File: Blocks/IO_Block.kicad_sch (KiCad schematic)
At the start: 3 parts

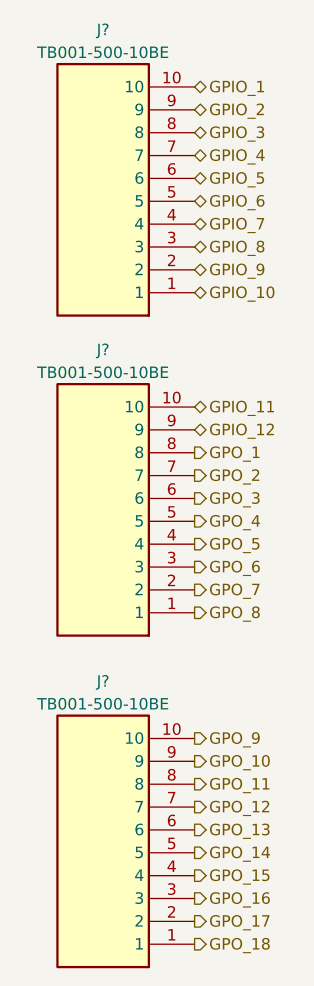
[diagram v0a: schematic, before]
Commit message: Automate library addition * Added script to automagically extract samacsys libraries and put them in corresponding folders. * Note: Requires zsh
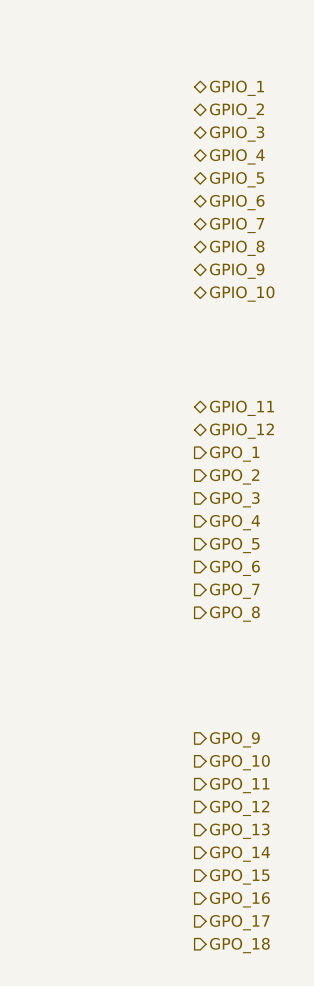
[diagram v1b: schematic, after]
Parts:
- removed J? (x3): TB001-500-10BE, LIB_TB001-500-10BE:SHDR10W100P0X500_1X10_5000X900X1250P, symbol TB001-500-10BE:TB001-500-10BE
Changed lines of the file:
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@@
     (effects (font (size 1.27 1.27)) (justify left))
   )
-  (symbol (lib_id "TB001-500-10BE:TB001-500-10BE") (at 86.36 153.67 180) (unit 1)
-    (in_bom yes) (on_board yes) (dnp no) (fields_autoplaced)
-    (property "Reference" "J?" (at 76.2 124.46 0)
-      (effects (font (size 1.27 1.27)))
-    )
-    (property "Value" "TB001-500-10BE" (at 76.2 127 0)
-      (effects (font (size 1.27 1.27)))
-    )
-    (property "Footprint" "LIB_TB001-500-10BE:SHDR10W100P0X500_1X10_5000X900X1250P" (at 69.85 58.75 0)
-      (effects (font (size 1.27 1.27)) (justify left top) hide)
-    )
-    (property "Datasheet" "https://componentsearchengine.com/Datasheets/1/TB001-500-10BE.pdf" (at 69.85 -41.25 0)
-      (effects (font (size 1.27 1.27)) (justify left top) hide)
-    )
-    (property "Height" "12.5" (at 69.85 -241.25 0)
-      (effects (font (size 1.27 1.27)) (justify left top) hide)
-    )
-    (property "Mouser Part Number" "490-TB001-500-10BE" (at 69.85 -341.25 0)
-      (effects (font (size 1.27 1.27)) (justify left top) hide)
-    )
-    (property "Mouser Price/Stock" "https://www.mouser.co.uk/ProductDetail/CUI-Devices/TB001-500-10BE?qs=vLWxofP3U2zH1ZAwWBP5mg%3D%3D" (at 69.85 -441.25 0)
-      (effects (font (size 1.27 1.27)) (justify left top) hide)
-    )
-    (property "Manufacturer_Name" "CUI Devices" (at 69.85 -541.25 0)
-      (effects (font (size 1.27 1.27)) (justify left top) hide)
-    )
-    (property "Manufacturer_Part_Number" "TB001-500-10BE" (at 69.85 -641.25 0)
-      (effects (font (size 1.27 1.27)) (justify left top) hide)
-    )
-    (pin "1")
-    (pin "10")
-    (pin "2")
-    (pin "3")
-    (pin "4")
-    (pin "5")
-    (pin "6")
-    (pin "7")
-    (pin "8")
-    (pin "9")
-    (instances
-      (project "PLC-CIM"
-        (path "/98f81d77-8880-491b-a7cf-4c27e2d73edf"
-          (reference "J?") (unit 1)
-        )
-        (path "/98f81d77-8880-491b-a7cf-4c27e2d73edf/ef38368d-af5e-44c5-8106-4a2f4dcc6c35"
-          (reference "J3") (unit 1)
-        )
-      )
-    )
-  )
-  (symbol (lib_id "TB001-500-10BE:TB001-500-10BE") (at 86.36 116.84 180) (unit 1)
-    (in_bom yes) (on_board yes) (dnp no) (fields_autoplaced)
-    (property "Reference" "J?" (at 76.2 87.63 0)
-      (effects (font (size 1.27 1.27)))
-    )
-    (property "Value" "TB001-500-10BE" (at 76.2 90.17 0)
-      (effects (font (size 1.27 1.27)))
-    )
-    (property "Footprint" "LIB_TB001-500-10BE:SHDR10W100P0X500_1X10_5000X900X1250P" (at 69.85 21.92 0)
-      (effects (font (size 1.27 1.27)) (justify left top) hide)
-    )
-    (property "Datasheet" "https://componentsearchengine.com/Datasheets/1/TB001-500-10BE.pdf" (at 69.85 -78.08 0)
-      (effects (font (size 1.27 1.27)) (justify left top) hide)
-    )
-    (property "Height" "12.5" (at 69.85 -278.08 0)
-      (effects (font (size 1.27 1.27)) (justify left top) hide)
-    )
-    (property "Mouser Part Number" "490-TB001-500-10BE" (at 69.85 -378.08 0)
-      (effects (font (size 1.27 1.27)) (justify left top) hide)
-    )
-    (property "Mouser Price/Stock" "https://www.mouser.co.uk/ProductDetail/CUI-Devices/TB001-500-10BE?qs=vLWxofP3U2zH1ZAwWBP5mg%3D%3D" (at 69.85 -478.08 0)
-      (effects (font (size 1.27 1.27)) (justify left top) hide)
-    )
-    (property "Manufacturer_Name" "CUI Devices" (at 69.85 -578.08 0)
-      (effects (font (size 1.27 1.27)) (justify left top) hide)
-    )
-    (property "Manufacturer_Part_Number" "TB001-500-10BE" (at 69.85 -678.08 0)
-      (effects (font (size 1.27 1.27)) (justify left top) hide)
-    )
-    (pin "1")
-    (pin "10")
-    (pin "2")
-    (pin "3")
-    (pin "4")
-    (pin "5")
-    (pin "6")
-    (pin "7")
-    (pin "8")
-    (pin "9")
-    (instances
-      (project "PLC-CIM"
-        (path "/98f81d77-8880-491b-a7cf-4c27e2d73edf"
-          (reference "J?") (unit 1)
-        )
-        (path "/98f81d77-8880-491b-a7cf-4c27e2d73edf/ef38368d-af5e-44c5-8106-4a2f4dcc6c35"
-          (reference "J2") (unit 1)
-        )
-      )
-    )
-  )
-  (symbol (lib_id "TB001-500-10BE:TB001-500-10BE") (at 86.36 81.28 180) (unit 1)
-    (in_bom yes) (on_board yes) (dnp no) (fields_autoplaced)
-    (property "Reference" "J?" (at 76.2 52.07 0)
-      (effects (font (size 1.27 1.27)))
-    )
-    (property "Value" "TB001-500-10BE" (at 76.2 54.61 0)
-      (effects (font (size 1.27 1.27)))
-    )
-    (property "Footprint" "LIB_TB001-500-10BE:SHDR10W100P0X500_1X10_5000X900X1250P" (at 69.85 -13.64 0)
-      (effects (font (size 1.27 1.27)) (justify left top) hide)
-    )
-    (property "Datasheet" "https://componentsearchengine.com/Datasheets/1/TB001-500-10BE.pdf" (at 69.85 -113.64 0)
-      (effects (font (size 1.27 1.27)) (justify left top) hide)
-    )
-    (property "Height" "12.5" (at 69.85 -313.64 0)
-      (effects (font (size 1.27 1.27)) (justify left top) hide)
-    )
-    (property "Mouser Part Number" "490-TB001-500-10BE" (at 69.85 -413.64 0)
-      (effects (font (size 1.27 1.27)) (justify left top) hide)
-    )
-    (property "Mouser Price/Stock" "https://www.mouser.co.uk/ProductDetail/CUI-Devices/TB001-500-10BE?qs=vLWxofP3U2zH1ZAwWBP5mg%3D%3D" (at 69.85 -513.64 0)
-      (effects (font (size 1.27 1.27)) (justify left top) hide)
-    )
-    (property "Manufacturer_Name" "CUI Devices" (at 69.85 -613.64 0)
-      (effects (font (size 1.27 1.27)) (justify left top) hide)
-    )
-    (property "Manufacturer_Part_Number" "TB001-500-10BE" (at 69.85 -713.64 0)
-      (effects (font (size 1.27 1.27)) (justify left top) hide)
-    )
-    (pin "1")
-    (pin "10")
-    (pin "2")
-    (pin "3")
-    (pin "4")
-    (pin "5")
-    (pin "6")
-    (pin "7")
-    (pin "8")
-    (pin "9")
-    (instances
-      (project "PLC-CIM"
-        (path "/98f81d77-8880-491b-a7cf-4c27e2d73edf"
-          (reference "J?") (unit 1)
-        )
-        (path "/98f81d77-8880-491b-a7cf-4c27e2d73edf/ef38368d-af5e-44c5-8106-4a2f4dcc6c35"
-          (reference "J1") (unit 1)
-        )
-      )
-    )
-  )
 )
